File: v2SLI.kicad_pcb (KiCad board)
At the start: 2 copper layers, 77.7 x 75.9 mm, 60 parts, among them J1 Inter-MCU Interrupts Header, J10 Programming Header for 205, J11 Boot 0, J12 Boot 1, J13 Boot 1, J14 Programming Header for 103, J15 Boot 0, J16 SPI Bus, J17 Enable Fix, J18 GPIOs, J19 UART1, J2 Inter-MCU UART Header, J20 Micro_SD_Card, J21 Radio UART, J22 VCC RAIL, J23 GND RAIL, J3 SPI Bus, J4 UART1, J5 205GPIOs, J6 UART2, J7 I2C1, J8 Conn_02x15_Top_Bottom, J9 Conn_02x15_Top_Bottom, SW1 SW_Push, SW2 SW_Push, SW3 SW_Push, U1 STM32F205RETx, U2 BMP388, U3 BMP388, U4 ICM20948, U5 TCR2EE185-SOT553, U6 ADA746, U7 STM32F103C8Tx, U8 Xbee

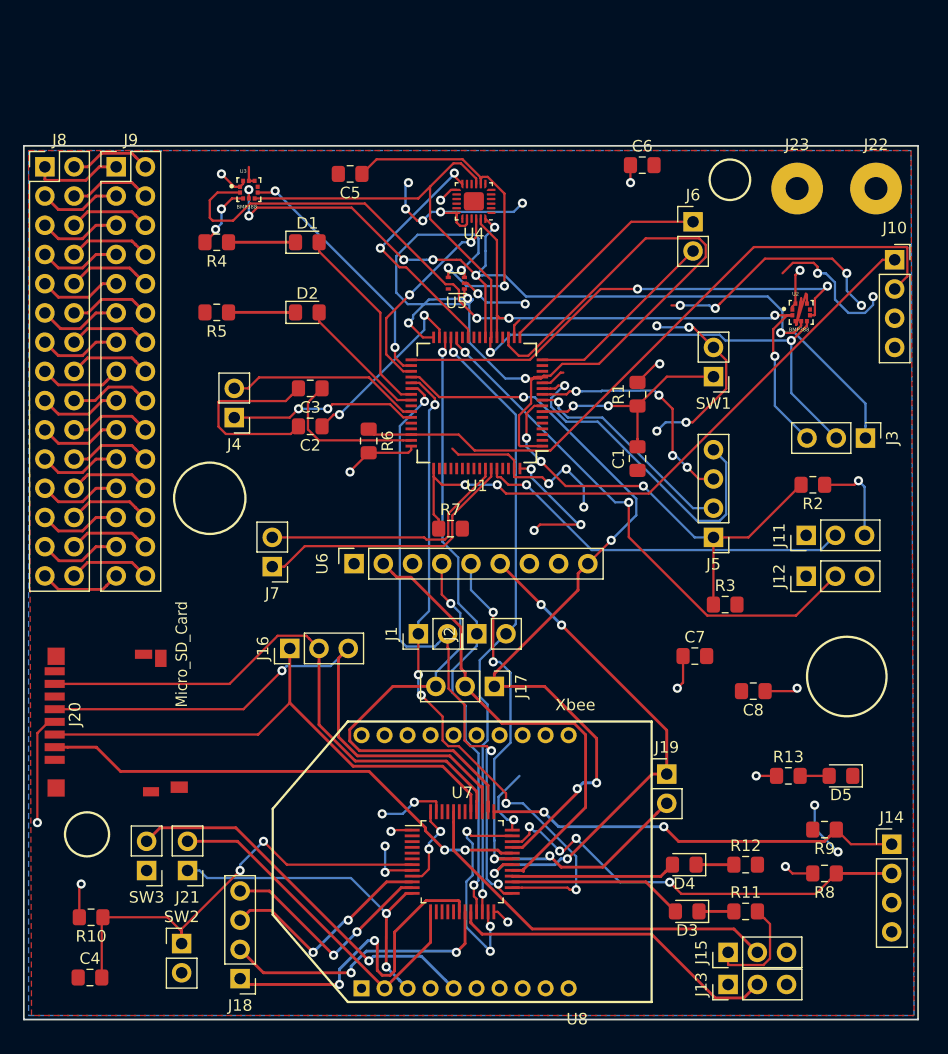
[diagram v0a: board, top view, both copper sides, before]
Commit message: added a zip of a few footprints that I hadn't proplery imported.
I designed this in a rush and didn't really bother to get the footprints properly in there, just got the same settings from SLI v1. Now I know for future projects
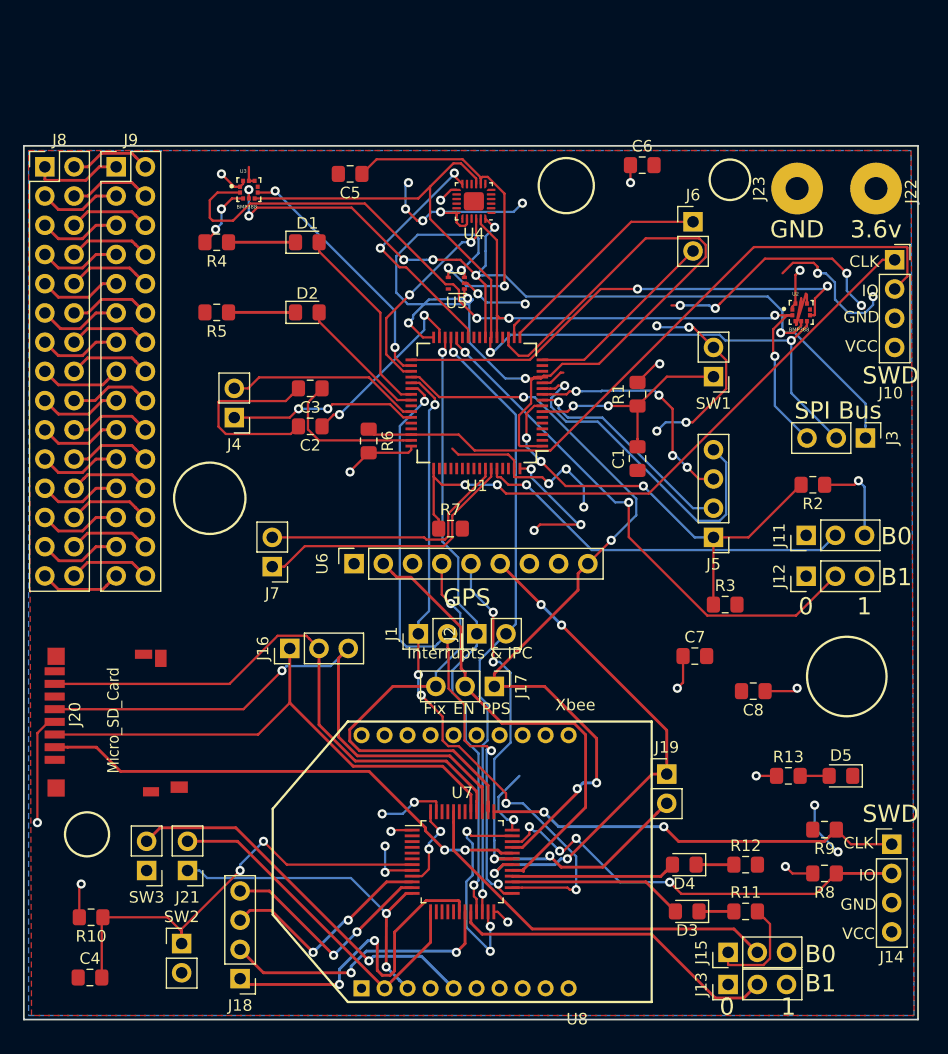
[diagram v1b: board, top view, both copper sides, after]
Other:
- board text added: "0"
- board text added: "1"
- board text added: "3.6v"
- board text added: "B0"
- board text added: "B1"
- board text added: "CLK"
- board text added: "EN"
- board text added: "Fix"
- board text added: "GND"
- board text added: "GPS"
- board text added: "IO"
- board text added: "Interrupts & IPC"
- board text added: "PPS"
- board text added: "SPI Bus"
- board text added: "SWD"
- board text added: "VCC"
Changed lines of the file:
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@@
   (general
     (thickness 1.6)
-    (drawings 10)
+    (drawings 37)
     (tracks 1114)
     (zones 0)
@@
     (descr "Through hole straight socket strip, 1x04, 2.54mm pitch, single row (from Kicad 4.0.7), script generated")
     (tags "Through hole socket strip THT 1x04 2.54mm single row")
-    (fp_text reference J10 (at 0 -2.77) (layer F.SilkS)
+    (fp_text reference J10 (at -0.351741 11.586259) (layer F.SilkS)
       (effects (font (size 1 1) (thickness 0.15)))
     )
@@
     (descr "Through hole straight pin header, 1x04, 2.54mm pitch, single row")
     (tags "Through hole pin header THT 1x04 2.54mm single row")
-    (fp_text reference J14 (at 0 -2.33) (layer F.SilkS)
+    (fp_text reference J14 (at 0 9.808259) (layer F.SilkS)
       (effects (font (size 1 1) (thickness 0.15)))
     )
@@
       (effects (font (size 1.00061 1.00061) (thickness 0.05)))
     )
-    (fp_text value Micro_SD_Card (at 0 0 270) (layer F.SilkS)
+    (fp_text value Micro_SD_Card (at 5.744259 5.939741 270) (layer F.SilkS)
       (effects (font (size 1 0.9) (thickness 0.05)))
     )
@@
     (tags "LED handsolder")
     (attr smd)
-    (fp_text reference D5 (at 0 -1.65 180) (layer F.SilkS)
+    (fp_text reference D5 (at 0 1.778 180) (layer F.SilkS)
       (effects (font (size 1 1) (thickness 0.15)))
     )
@@
     (tags connector)
     (attr virtual)
-    (fp_text reference J22 (at 0 -3.81) (layer F.SilkS)
+    (fp_text reference J22 (at 3.048 0.254 90) (layer F.SilkS)
       (effects (font (size 1 1) (thickness 0.15)))
     )
@@
     (tags connector)
     (attr virtual)
-    (fp_text reference J23 (at 0 -3.81) (layer F.SilkS)
+    (fp_text reference J23 (at -3.302 0 90) (layer F.SilkS)
       (effects (font (size 1 1) (thickness 0.15)))
     )
@@
       (net 2 GND))
   )
+  (gr_text PPS (at 165.510259 81.944259) (layer F.SilkS)
+    (effects (font (size 1 1) (thickness 0.2)))
+  )
+  (gr_text EN (at 162.716259 81.944259) (layer F.SilkS)
+    (effects (font (size 1 1) (thickness 0.2)))
+  )
+  (gr_text Fix (at 160.176259 81.944259) (layer F.SilkS)
+    (effects (font (size 1 1) (thickness 0.2)))
+  )
+  (gr_text "Interrupts & IPC" (at 163.224259 77.118259) (layer F.SilkS)
+    (effects (font (size 1 1) (thickness 0.2)))
+  )
+  (gr_text GPS (at 162.970259 72.292259) (layer F.SilkS)
+    (effects (font (size 1.5 1.5) (thickness 0.3)))
+  )
+  (gr_text 3.6v (at 198.530259 40.288259) (layer F.SilkS)
+    (effects (font (size 1.5 1.5) (thickness 0.3)))
+  )
+  (gr_text GND (at 191.672259 40.288259) (layer F.SilkS)
+    (effects (font (size 1.5 1.5) (thickness 0.3)))
+  )
+  (gr_text SWD (at 199.800259 52.988259) (layer F.SilkS)
+    (effects (font (size 1.5 1.5) (thickness 0.3)))
+  )
+  (gr_text CLK (at 197.514259 43.082259) (layer F.SilkS)
+    (effects (font (size 1 1) (thickness 0.2)))
+  )
+  (gr_text IO (at 198.022259 45.622259) (layer F.SilkS)
+    (effects (font (size 1 1) (thickness 0.2)))
+  )
+  (gr_text VCC (at 197.260259 50.448259) (layer F.SilkS)
+    (effects (font (size 1 1) (thickness 0.2)))
+  )
+  (gr_text GND (at 197.260259 47.908259) (layer F.SilkS)
+    (effects (font (size 1 1) (thickness 0.2)))
+  )
+  (gr_text "SPI Bus" (at 195.228259 56.036259) (layer F.SilkS)
+    (effects (font (size 1.5 1.5) (thickness 0.3)))
+  )
+  (gr_text 1 (at 197.514259 73.054259) (layer F.SilkS)
+    (effects (font (size 1.5 1.5) (thickness 0.3)))
+  )
+  (gr_text 0 (at 192.434259 73.054259) (layer F.SilkS)
+    (effects (font (size 1.5 1.5) (thickness 0.3)))
+  )
+  (gr_text B1 (at 200.308259 70.514259) (layer F.SilkS)
+    (effects (font (size 1.5 1.5) (thickness 0.3)))
+  )
+  (gr_text B0 (at 200.308259 66.958259) (layer F.SilkS)
+    (effects (font (size 1.5 1.5) (thickness 0.3)))
+  )
+  (gr_text SWD (at 199.800259 91.088259) (layer F.SilkS)
+    (effects (font (size 1.5 1.5) (thickness 0.3)))
+  )
+  (gr_text CLK (at 197.006259 93.628259) (layer F.SilkS)
+    (effects (font (size 1 1) (thickness 0.2)))
+  )
+  (gr_text IO (at 197.768259 96.422259) (layer F.SilkS)
+    (effects (font (size 1 1) (thickness 0.2)))
+  )
+  (gr_text GND (at 197.006259 98.962259) (layer F.SilkS)
+    (effects (font (size 1 1) (thickness 0.2)))
+  )
+  (gr_text VCC (at 197.006259 101.502259) (layer F.SilkS)
+    (effects (font (size 1 1) (thickness 0.2)))
+  )
+  (gr_text 1 (at 190.910259 107.852259) (layer F.SilkS)
+    (effects (font (size 1.5 1.5) (thickness 0.3)))
+  )
+  (gr_text 0 (at 185.576259 107.852259) (layer F.SilkS)
+    (effects (font (size 1.5 1.5) (thickness 0.3)))
+  )
+  (gr_text "B1\n" (at 193.704259 105.820259) (layer F.SilkS)
+    (effects (font (size 1.5 1.5) (thickness 0.3)))
+  )
+  (gr_text B0 (at 193.704259 103.280259) (layer F.SilkS)
+    (effects (font (size 1.5 1.5) (thickness 0.3)))
+  )
+  (gr_circle (center 171.606259 36.478259) (end 173.638259 37.748259) (layer F.SilkS) (width 0.2))
   (dimension 75.946 (width 0.3) (layer F.SilkS)
     (gr_text "75.946 mm" (at 216.886259 70.895259 270) (layer F.SilkS)

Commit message: added some rando holes, will adjust when I talk to jonny
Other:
- board size 77.7 x 75.9 mm -> 77.7 x 86.5 mm
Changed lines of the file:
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@@
   (general
     (thickness 1.6)
-    (drawings 37)
+    (drawings 40)
     (tracks 1114)
     (zones 0)
@@
     (trace_min 0.2)
     (segment_width 0.2)
-    (edge_width 0.15)
+    (edge_width 0.2)
     (via_size 0.8)
     (via_drill 0.4)
@@
       (net 2 GND))
   )
+  (gr_circle (center 190.148259 28.096259) (end 191.735759 28.096259) (layer Edge.Cuts) (width 0.2))
+  (gr_circle (center 183.036259 24.032259) (end 184.623759 24.032259) (layer Edge.Cuts) (width 0.2))
+  (gr_circle (center 172.368259 37.240259) (end 173.955759 37.240259) (layer Edge.Cuts) (width 0.2))
   (gr_text PPS (at 165.510259 81.944259) (layer F.SilkS)
     (effects (font (size 1 1) (thickness 0.2)))
@@
     (effects (font (size 1.5 1.5) (thickness 0.3)))
   )
-  (gr_circle (center 171.606259 36.478259) (end 173.638259 37.748259) (layer F.SilkS) (width 0.2))
+  (gr_circle (center 172.364563 37.240259) (end 175.158563 37.09649) (layer F.SilkS) (width 0.2))
   (dimension 75.946 (width 0.3) (layer F.SilkS)
     (gr_text "75.946 mm" (at 216.886259 70.895259 270) (layer F.SilkS)
@@
   )
   (gr_circle (center 129.950259 92.866259) (end 129.188259 94.623166) (layer F.SilkS) (width 0.2))
-  (gr_circle (center 185.830259 35.970259) (end 187.354259 36.851649) (layer F.SilkS) (width 0.2))
+  (gr_circle (center 185.258759 35.716259) (end 186.846259 35.716259) (layer F.SilkS) (width 0.2))
   (gr_circle (center 195.990259 79.150259) (end 198.784259 81.182259) (layer F.SilkS) (width 0.2))
   (gr_circle (center 140.618259 63.656259) (end 143.158259 65.434259) (layer F.SilkS) (width 0.2))

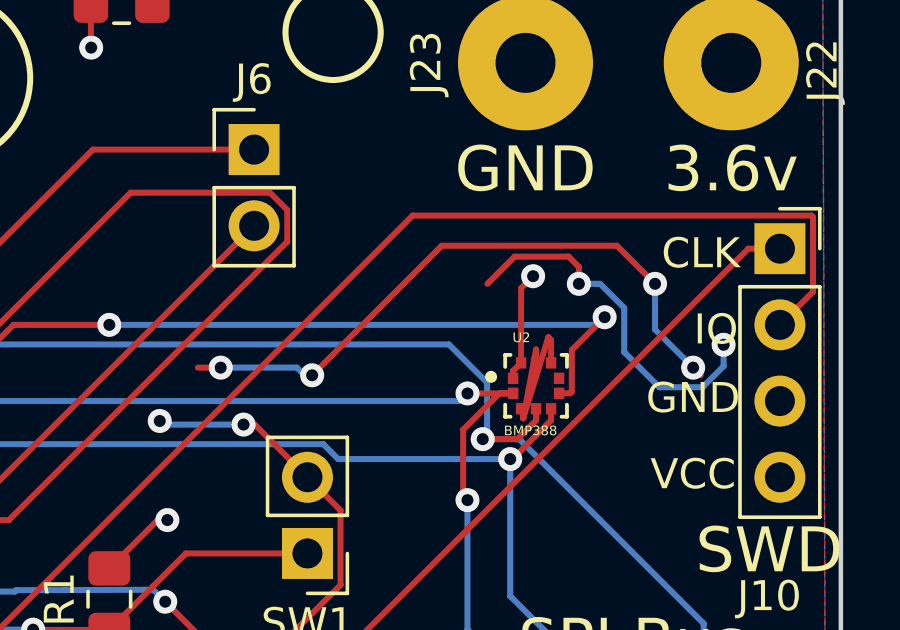
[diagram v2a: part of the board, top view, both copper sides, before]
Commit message: got rid of some unconnected stuff
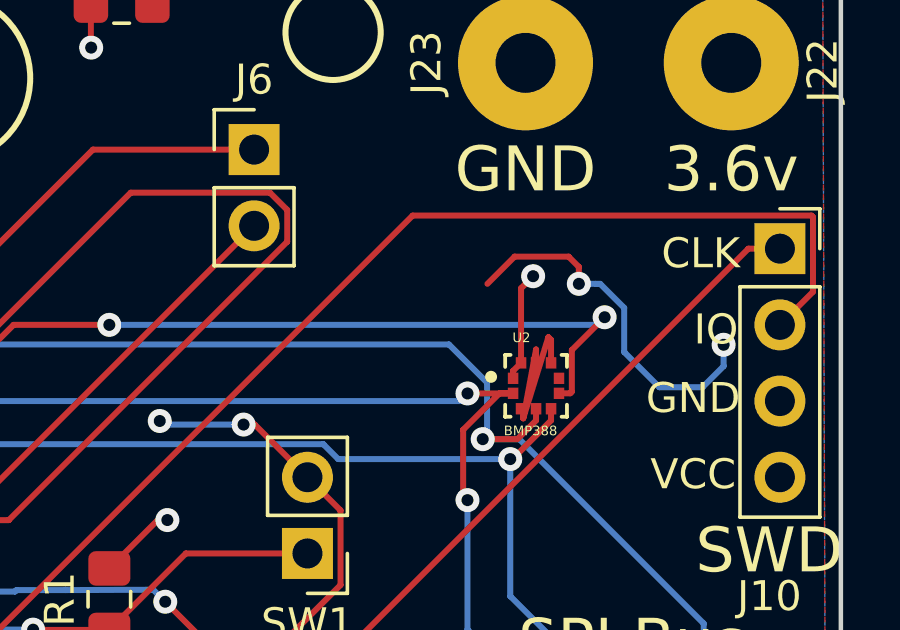
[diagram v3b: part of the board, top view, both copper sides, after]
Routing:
- net (no net): track 21.3 -> 0.00 mm, vias 4 -> 0
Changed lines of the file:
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@@
     (thickness 1.6)
     (drawings 40)
-    (tracks 1114)
+    (tracks 1099)
     (zones 0)
     (modules 60)
@@
   (gr_line (start 124.46 108.966) (end 202.184 108.966) (layer Edge.Cuts) (width 0.15))
   (gr_line (start 124.46 33.02) (end 124.46 108.966) (layer Edge.Cuts) (width 0.15))
-  (via (at 181.512259 46.892259) (size 0.8) (drill 0.4) (layers F.Cu B.Cu) (net 0))
-  (segment (start 180.750259 46.892259) (end 181.512259 46.892259) (width 0.2) (layer F.Cu) (net 0))
-  (segment (start 181.512259 46.892259) (end 184.052259 46.892259) (width 0.2) (layer B.Cu) (net 0))
-  (via (at 184.560259 47.146259) (size 0.8) (drill 0.4) (layers F.Cu B.Cu) (net 0))
-  (segment (start 184.306259 47.146259) (end 184.560259 47.146259) (width 0.2) (layer B.Cu) (net 0))
-  (segment (start 184.052259 46.892259) (end 184.306259 47.146259) (width 0.2) (layer B.Cu) (net 0))
-  (via (at 197.260259 46.892259) (size 0.8) (drill 0.4) (layers F.Cu B.Cu) (net 0))
-  (segment (start 197.514259 47.146259) (end 197.260259 46.892259) (width 0.2) (layer F.Cu) (net 0))
-  (segment (start 197.260259 46.892259) (end 195.990259 45.622259) (width 0.2) (layer B.Cu) (net 0))
-  (via (at 195.990259 44.098259) (size 0.8) (drill 0.4) (layers F.Cu B.Cu) (net 0))
-  (segment (start 195.990259 45.622259) (end 195.990259 44.098259) (width 0.2) (layer B.Cu) (net 0))
-  (segment (start 184.960258 46.74626) (end 184.560259 47.146259) (width 0.2) (layer F.Cu) (net 0))
-  (segment (start 194.720259 42.828259) (end 188.878259 42.828259) (width 0.2) (layer F.Cu) (net 0))
-  (segment (start 188.878259 42.828259) (end 184.960258 46.74626) (width 0.2) (layer F.Cu) (net 0))
-  (segment (start 195.990259 44.098259) (end 194.720259 42.828259) (width 0.2) (layer F.Cu) (net 0))
   (segment (start 177.8 58.507) (end 177.8 55.635) (width 0.2) (layer F.Cu) (net 1))
   (segment (start 177.8 59.182) (end 177.8 58.507) (width 0.2) (layer F.Cu) (net 1))

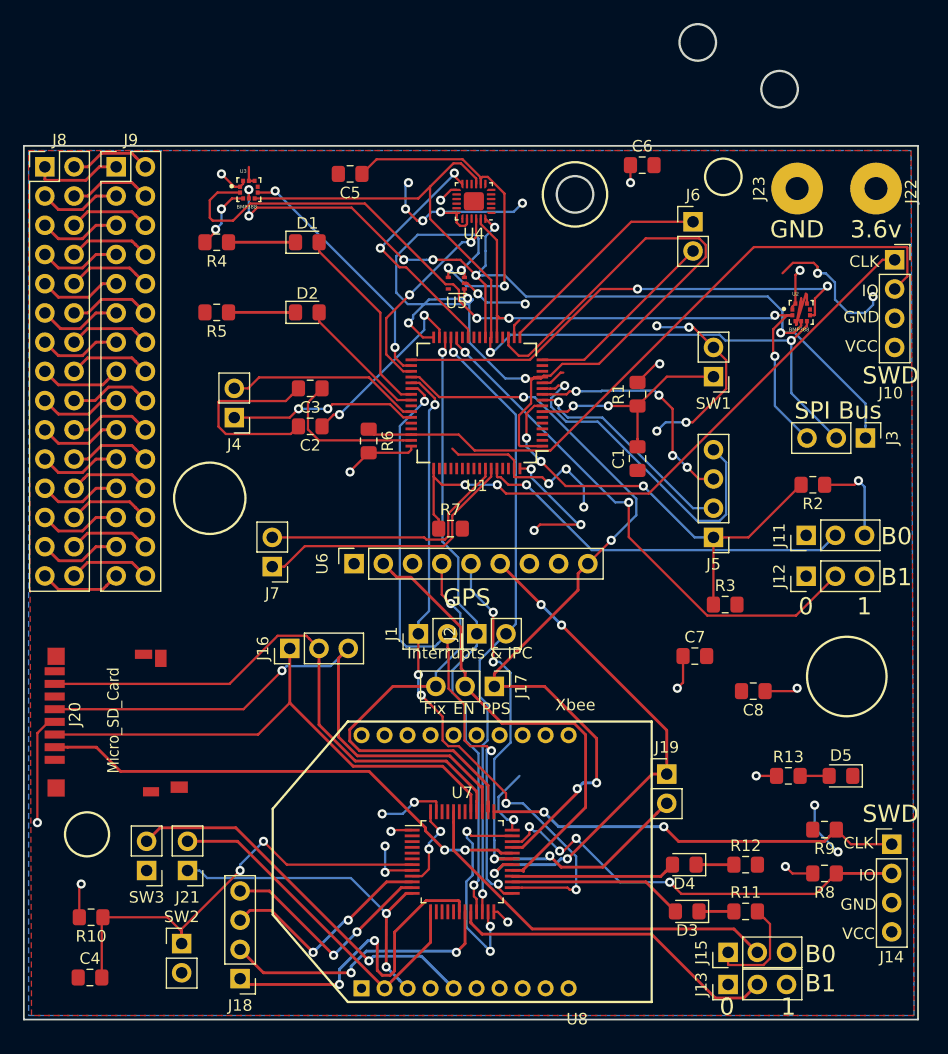
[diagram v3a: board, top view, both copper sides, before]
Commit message: Ran DRC, no major fixable issues. Via near track for VDDIO and VCC, this may be a problem but unlikely given the manufacturers we'll be using
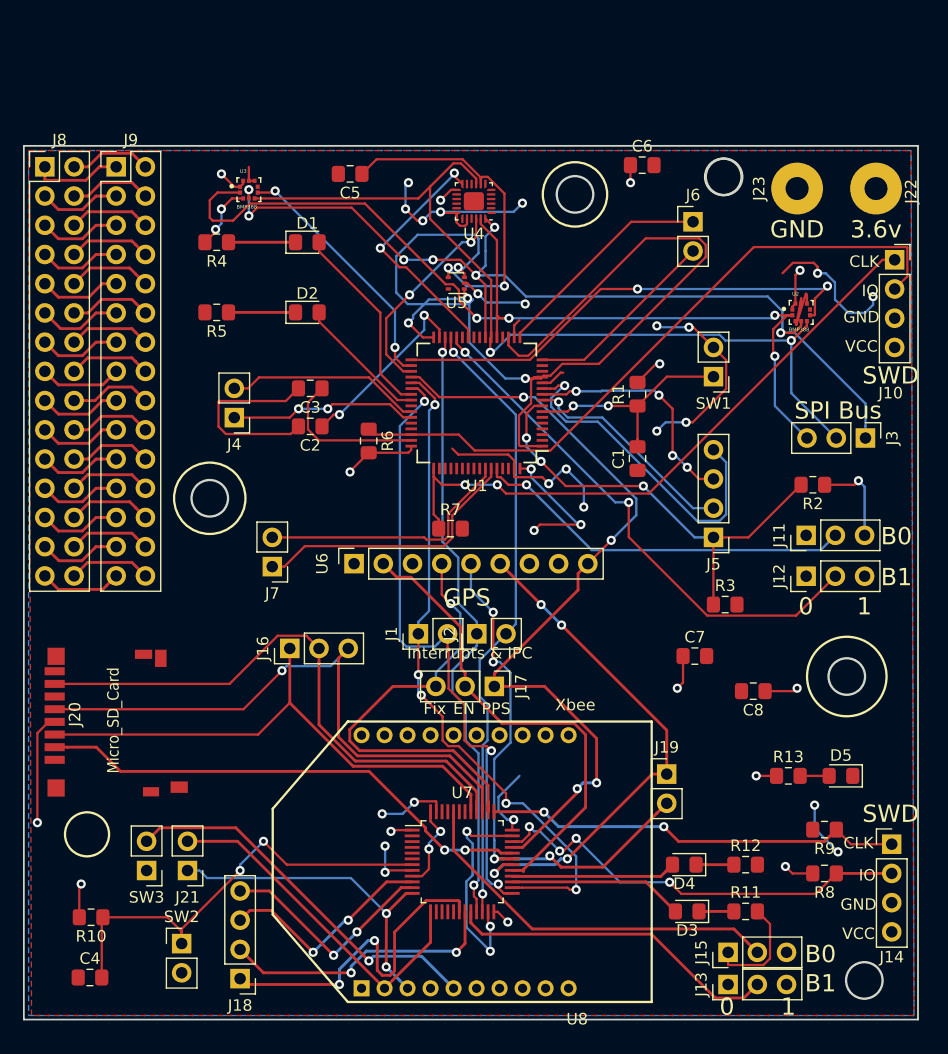
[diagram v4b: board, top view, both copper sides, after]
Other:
- board size 77.7 x 86.5 mm -> 77.7 x 75.9 mm
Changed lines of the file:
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@@
   (general
     (thickness 1.6)
-    (drawings 40)
+    (drawings 42)
     (tracks 1099)
     (zones 0)
@@
       (net 2 GND))
   )
-  (gr_circle (center 190.148259 28.096259) (end 191.735759 28.096259) (layer Edge.Cuts) (width 0.2))
-  (gr_circle (center 183.036259 24.032259) (end 184.623759 24.032259) (layer Edge.Cuts) (width 0.2))
+  (gr_circle (center 197.514259 105.566259) (end 199.101759 105.566259) (layer Edge.Cuts) (width 0.2))
+  (gr_circle (center 195.990259 79.150259) (end 197.577759 79.150259) (layer Edge.Cuts) (width 0.2))
+  (gr_circle (center 185.322259 35.716259) (end 186.909759 35.716259) (layer Edge.Cuts) (width 0.2))
+  (gr_circle (center 140.618259 63.656259) (end 142.205759 63.656259) (layer Edge.Cuts) (width 0.2))
   (gr_circle (center 172.368259 37.240259) (end 173.955759 37.240259) (layer Edge.Cuts) (width 0.2))
   (gr_text PPS (at 165.510259 81.944259) (layer F.SilkS)
@@
   (segment (start 154.905 58.122) (end 154.432 57.649) (width 0.2) (layer F.Cu) (net 62))
   (segment (start 158.13 58.122) (end 154.905 58.122) (width 0.2) (layer F.Cu) (net 62))
-  (segment (start 162.752 44.108) (end 162.488259 43.844259) (width 0.2) (layer F.Cu) (net 63))
   (segment (start 162.752 44.458) (end 162.752 44.108) (width 0.2) (layer F.Cu) (net 63))
-  (segment (start 162.488259 43.844259) (end 162.488259 43.844259) (width 0.2) (layer F.Cu) (net 63))
-  (via (at 162.488259 43.844259) (size 0.8) (drill 0.4) (layers F.Cu B.Cu) (net 63))
+  (via (at 162.208259 43.590259) (size 0.8) (drill 0.4) (layers F.Cu B.Cu) (net 63))
   (via (at 160.684259 37.748259) (size 0.8) (drill 0.4) (layers F.Cu B.Cu) (net 63))
   (segment (start 161.586518 36.846) (end 160.684259 37.748259) (width 0.2) (layer F.Cu) (net 63))
@@
   (segment (start 191.259 46.998) (end 191.524 46.733) (width 0.2) (layer F.Cu) (net 63))
   (segment (start 191.259 47.248) (end 191.259 46.998) (width 0.2) (layer F.Cu) (net 63))
+  (segment (start 162.726 44.108) (end 162.208259 43.590259) (width 0.2) (layer F.Cu) (net 63))
+  (segment (start 162.752 44.108) (end 162.726 44.108) (width 0.2) (layer F.Cu) (net 63))
   (via (at 168.148 62.484) (size 0.8) (drill 0.4) (layers F.Cu B.Cu) (net 64))
   (segment (start 173.823001 68.159001) (end 168.148 62.484) (width 0.2) (layer B.Cu) (net 64))

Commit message: added some images from images library
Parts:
- added G***: LOGO, images:everybody, B.Cu at (164.2, 90.6)
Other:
- board text added: "Dhruv Gramopadhye, Class of 2020 https://github.com/dgramop/v2SLI"
- board text added: "Mounting Headers"
- board text added: "Oakton High School Rocketry"
